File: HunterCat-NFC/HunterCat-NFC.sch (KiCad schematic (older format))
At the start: 66 parts, among them J1 Battery, J2 Breakout Conn, P1 USB_C_Plug_USB2.0, SW1 RESET, U1 ATSAMD21E18A, U2 PN7150B0HN_C11002E-PN7150B0HN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, U3 MCP73831-3-OT, U4 AP2112K-3.3, U5 GD25Q16CSIGR, Y1 27.12Mhz

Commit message: manf#
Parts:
- C1, C25: manf# (none) -> C0805C104K5RAC7800
- C10, C11: manf# (none) -> ECHU1C102GX5
- C12, C13: manf# (none) -> C1608NP0681JGT
- C14, C18: manf# (none) -> CL10C560JB8NNNC
- C15, C17: manf# (none) -> GRM1882C1H220JA01D
- C16, C23, C24: manf# (none) -> CL21A106KOQNNNG
- C19, C20: manf# (none) -> C1608C0G2E121JT000N
- C2, C5, C6, C8: manf# (none) -> 0805B105K500AT
- C21, C22: manf# (none) -> CL10C2R2BB8NNNC
- C3, C4: manf# (none) -> 0805CG100J500NT
- C7, C9: manf# (none) -> CL21B104KBCNNNC
- D1: manf# (none) -> R080508L3
- D2, D3: manf# (none) -> ORH-B35A
- D4: manf# (none) -> 2012HYK-588J
- F1: manf# (none) -> MFU0805FF00500P100
- L1, L2: manf# (none) -> MLJ1608WR16JT000
- P1: manf# (none) -> TYPE-C16PIN
- R1, R16, R2, R21: manf# (none) -> 0805W8J0103T5E
- R10, R12, R17, R18, R4: manf# (none) -> 0805W8J0102T5E
- R11, R13: manf# (none) -> RK73B1JTTD222J
- R14, R15: manf# (none) -> RC0603FR-073R4L
- R19, R20, R3, R5, R6, R7: manf# (none) -> ERJ6RBD1003V
- R8, R9: manf# (none) -> 0805W8J0512T5E
- SW1: manf# (none) -> TS-1187A-C-C-B
- U1: manf# (none) -> ATSAMD21E18A-AU
- U2: manf# (none) -> PN7150B0HN/C11002
- U3: manf# (none) -> MCP73831-3-OT
- U4: manf# (none) -> AP2112K-3.3
- U5: manf# (none) -> GD25Q16CSIGR
- Y1: manf# (none) -> X3S027120BA1H-X

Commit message: change manf#
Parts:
- C1, C25: manf# C0805C104K5RAC7800 -> 885012207072
- C10, C11: manf# ECHU1C102GX5 -> CC0201JRX7R7BB102
- C12, C13: manf# C1608NP0681JGT -> 885012206107
- C14, C18: manf# CL10C560JB8NNNC -> GRM0335C1H560FA01D
- C15, C17: manf# GRM1882C1H220JA01D -> 06035A220JAT4A
- C16, C23, C24: manf# CL21A106KOQNNNG -> C0805C106K9PACTU
- C19, C20: manf# C1608C0G2E121JT000N -> C0603C121J5GAC
- C2, C5, C6, C8: manf# 0805B105K500AT -> 885012207078
- C21, C22: manf# CL10C2R2BB8NNNC -> GCM0335C1E2R2CA16D
- C3, C4: manf# 0805CG100J500NT -> 885012007076
- C7, C9: manf# CL21B104KBCNNNC -> 885012207072
- R1, R16, R2, R21: manf# 0805W8J0103T5E -> CRCW080510K0JNEAC
- R10, R12, R17, R18, R4: manf# 0805W8J0102T5E -> CRCW08051K50FKEAC
- R11, R13: manf# RK73B1JTTD222J -> RC0603JR-072K2L
- R3, R5, R6, R7: manf# ERJ6RBD1003V -> CRCW0805100KFKEAC
- R8, R9: manf# 0805W8J0512T5E -> CR0805-FX-5101ELF

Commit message: Change sch
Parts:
- added GPIO1: RESET, Button_Switch_SMD:SW_SPST_TL3342, symbol Switch:SW_Push
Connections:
- net GND: now also GPIO1.1
- net GPIO: now reaches U1.17 (PA16/I2C/EINT0/SERCOM1+3.0)
- net GPIO: now also GPIO1.2
- no-connect marks 10 -> 9
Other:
- moved on the sheet: D1, D3, D4, R17, R18, R4, SW1
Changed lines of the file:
@@
 EESchema Schematic File Version 4
-LIBS:HunterCat-NFC-cache
 EELAYER 30 0
 EELAYER END
@@
 L Switch:SW_Push SW1
 U 1 1 5E4BA999
-P 4665 3790
-F 0 "SW1" H 4665 4075 50  0000 C CNN
-F 1 "RESET" H 4665 3984 50  0000 C CNN
-F 2 "Button_Switch_SMD:SW_SPST_TL3342" H 4665 3990 50  0001 C CNN
-F 3 "~" H 4665 3990 50  0001 C CNN
-F 4 "TS-1187A-C-C-B" H 4665 3790 50  0001 C CNN "manf#"
-	1    4665 3790
+P 4640 3765
+F 0 "SW1" H 4640 4050 50  0000 C CNN
+F 1 "RESET" H 4640 3959 50  0000 C CNN
+F 2 "Button_Switch_SMD:SW_SPST_TL3342" H 4640 3965 50  0001 C CNN
+F 3 "~" H 4640 3965 50  0001 C CNN
+F 4 "TS-1187A-C-C-B" H 4640 3765 50  0001 C CNN "manf#"
+	1    4640 3765
 	1    0    0    -1
 $EndComp
@@
 L Device:LED D1
 U 1 1 5E4BB3C2
-P 4735 4380
-F 0 "D1" H 4728 4596 50  0000 C CNN
-F 1 "LED" H 4728 4505 50  0000 C CNN
-F 2 "LED_SMD:LED_0805_2012Metric_Pad1.15x1.40mm_HandSolder" H 4735 4380 50  0001 C CNN
-F 3 "~" H 4735 4380 50  0001 C CNN
-F 4 "R080508L3" H 4735 4380 50  0001 C CNN "manf#"
-	1    4735 4380
+P 4585 4780
+F 0 "D1" H 4578 4996 50  0000 C CNN
+F 1 "LED" H 4578 4905 50  0000 C CNN
+F 2 "LED_SMD:LED_0805_2012Metric_Pad1.15x1.40mm_HandSolder" H 4585 4780 50  0001 C CNN
+F 3 "~" H 4585 4780 50  0001 C CNN
+F 4 "R080508L3" H 4585 4780 50  0001 C CNN "manf#"
+	1    4585 4780
 	1    0    0    -1
 $EndComp
@@
 L Device:R_Small R4
 U 1 1 5E4BBC69
-P 4405 4380
-F 0 "R4" V 4209 4380 50  0000 C CNN
-F 1 "1K" V 4300 4380 50  0000 C CNN
-F 2 "Resistor_SMD:R_0805_2012Metric_Pad1.15x1.40mm_HandSolder" H 4405 4380 50  0001 C CNN
-F 3 "~" H 4405 4380 50  0001 C CNN
-F 4 "CRCW08051K50FKEAC" H 4405 4380 50  0001 C CNN "manf#"
-	1    4405 4380
+P 4255 4780
+F 0 "R4" V 4059 4780 50  0000 C CNN
+F 1 "1K" V 4150 4780 50  0000 C CNN
+F 2 "Resistor_SMD:R_0805_2012Metric_Pad1.15x1.40mm_HandSolder" H 4255 4780 50  0001 C CNN
+F 3 "~" H 4255 4780 50  0001 C CNN
+F 4 "CRCW08051K50FKEAC" H 4255 4780 50  0001 C CNN "manf#"
+	1    4255 4780
 	0    1    1    0
 $EndComp
 Wire Wire Line
-	4585 4380 4505 4380
-Wire Wire Line
-	4305 4380 4210 4380
-Wire Wire Line
-	4210 4380 4210 4420
-Wire Wire Line
-	4885 4380 4965 4380
+	4435 4780 4355 4780
+Wire Wire Line
+	4155 4780 4060 4780
+Wire Wire Line
+	4060 4780 4060 4820
+Wire Wire Line
+	4735 4780 4815 4780
 $Comp
 L power:GND #PWR011
 U 1 1 5E4CF1CD
-P 4210 4420
-F 0 "#PWR011" H 4210 4170 50  0001 C CNN
-F 1 "GND" H 4215 4247 50  0000 C CNN
-F 2 "" H 4210 4420 50  0001 C CNN
-F 3 "" H 4210 4420 50  0001 C CNN
-	1    4210 4420
-	1    0    0    -1
-$EndComp
-Text Label 4965 4380 0    50   ~ 0
+P 4060 4820
+F 0 "#PWR011" H 4060 4570 50  0001 C CNN
+F 1 "GND" H 4065 4647 50  0000 C CNN
+F 2 "" H 4060 4820 50  0001 C CNN
+F 3 "" H 4060 4820 50  0001 C CNN
+	1    4060 4820
+	1    0    0    -1
+$EndComp
+Text Label 4815 4780 0    50   ~ 0
 LED1
 Wire Wire Line
@@
 LED1
 Wire Wire Line
-	4465 3790 4385 3790
-Wire Wire Line
-	4385 3790 4385 3825
-Wire Wire Line
-	4865 3790 4940 3790
-Text Label 4940 3790 0    50   ~ 0
+	4440 3765 4360 3765
+Wire Wire Line
+	4360 3765 4360 3800
+Wire Wire Line
+	4840 3765 4915 3765
+Text Label 4915 3765 0    50   ~ 0
 RESET
 $Comp
 L power:GND #PWR013
 U 1 1 5E4EA915
-P 4385 3825
-F 0 "#PWR013" H 4385 3575 50  0001 C CNN
-F 1 "GND" H 4390 3652 50  0000 C CNN
-F 2 "" H 4385 3825 50  0001 C CNN
-F 3 "" H 4385 3825 50  0001 C CNN
-	1    4385 3825
+P 4360 3800
+F 0 "#PWR013" H 4360 3550 50  0001 C CNN
+F 1 "GND" H 4365 3627 50  0000 C CNN
+F 2 "" H 4360 3800 50  0001 C CNN
+F 3 "" H 4360 3800 50  0001 C CNN
+	1    4360 3800
 	1    0    0    -1
 $EndComp
@@
 L Device:LED D3
 U 1 1 5E770C69
-P 4750 4810
-F 0 "D3" H 4743 5026 50  0000 C CNN
-F 1 "LED" H 4743 4935 50  0000 C CNN
-F 2 "LED_SMD:LED_0805_2012Metric_Pad1.15x1.40mm_HandSolder" H 4750 4810 50  0001 C CNN
-F 3 "~" H 4750 4810 50  0001 C CNN
-F 4 "ORH-B35A" H 4750 4810 50  0001 C CNN "manf#"
-	1    4750 4810
+P 4620 5135
+F 0 "D3" H 4613 5351 50  0000 C CNN
+F 1 "LED" H 4613 5260 50  0000 C CNN
+F 2 "LED_SMD:LED_0805_2012Metric_Pad1.15x1.40mm_HandSolder" H 4620 5135 50  0001 C CNN
+F 3 "~" H 4620 5135 50  0001 C CNN
+F 4 "ORH-B35A" H 4620 5135 50  0001 C CNN "manf#"
+	1    4620 5135
 	1    0    0    -1
 $EndComp
@@
 L Device:R_Small R17
 U 1 1 5E770C6F
-P 4420 4810
-F 0 "R17" V 4224 4810 50  0000 C CNN
-F 1 "1K" V 4315 4810 50  0000 C CNN
-F 2 "Resistor_SMD:R_0805_2012Metric_Pad1.15x1.40mm_HandSolder" H 4420 4810 50  0001 C CNN
-F 3 "~" H 4420 4810 50  0001 C CNN
-F 4 "CRCW08051K50FKEAC" H 4420 4810 50  0001 C CNN "manf#"
-	1    4420 4810
+P 4290 5135
+F 0 "R17" V 4094 5135 50  0000 C CNN
+F 1 "1K" V 4185 5135 50  0000 C CNN
+F 2 "Resistor_SMD:R_0805_2012Metric_Pad1.15x1.40mm_HandSolder" H 4290 5135 50  0001 C CNN
+F 3 "~" H 4290 5135 50  0001 C CNN
+F 4 "CRCW08051K50FKEAC" H 4290 5135 50  0001 C CNN "manf#"
+	1    4290 5135
 	0    1    1    0
 $EndComp
 Wire Wire Line
-	4600 4810 4520 4810
-Wire Wire Line
-	4320 4810 4225 4810
-Wire Wire Line
-	4225 4810 4225 4850
-Wire Wire Line
-	4900 4810 4980 4810
+	4470 5135 4390 5135
+Wire Wire Line
+	4190 5135 4095 5135
+Wire Wire Line
+	4095 5135 4095 5175
+Wire Wire Line
+	4770 5135 4850 5135
 $Comp
 L power:GND #PWR0103
 U 1 1 5E770C79
-P 4225 4850
-F 0 "#PWR0103" H 4225 4600 50  0001 C CNN
-F 1 "GND" H 4230 4677 50  0000 C CNN
-F 2 "" H 4225 4850 50  0001 C CNN
-F 3 "" H 4225 4850 50  0001 C CNN
-	1    4225 4850
-	1    0    0    -1
-$EndComp
-Text Label 4980 4810 0    50   ~ 0
+P 4095 5175
+F 0 "#PWR0103" H 4095 4925 50  0001 C CNN
+F 1 "GND" H 4100 5002 50  0000 C CNN
+F 2 "" H 4095 5175 50  0001 C CNN
+F 3 "" H 4095 5175 50  0001 C CNN
+	1    4095 5175
+	1    0    0    -1
+$EndComp
+Text Label 4850 5135 0    50   ~ 0
 LED2
 $Comp
 L Device:LED D4
 U 1 1 5E793493
-P 4755 5355
-F 0 "D4" H 4748 5571 50  0000 C CNN
-F 1 "LED" H 4748 5480 50  0000 C CNN
-F 2 "LED_SMD:LED_0805_2012Metric_Pad1.15x1.40mm_HandSolder" H 4755 5355 50  0001 C CNN
-F 3 "~" H 4755 5355 50  0001 C CNN
-F 4 "2012HYK-588J" H 4755 5355 50  0001 C CNN "manf#"
-	1    4755 5355
+P 4645 5540
+F 0 "D4" H 4638 5756 50  0000 C CNN
+F 1 "LED" H 4638 5665 50  0000 C CNN
+F 2 "LED_SMD:LED_0805_2012Metric_Pad1.15x1.40mm_HandSolder" H 4645 5540 50  0001 C CNN
+F 3 "~" H 4645 5540 50  0001 C CNN
+F 4 "2012HYK-588J" H 4645 5540 50  0001 C CNN "manf#"
+	1    4645 5540
 	1    0    0    -1
 $EndComp
@@
 L Device:R_Small R18
 U 1 1 5E793499
-P 4425 5355
-F 0 "R18" V 4229 5355 50  0000 C CNN
-F 1 "1K" V 4320 5355 50  0000 C CNN
-F 2 "Resistor_SMD:R_0805_2012Metric_Pad1.15x1.40mm_HandSolder" H 4425 5355 50  0001 C CNN
-F 3 "~" H 4425 5355 50  0001 C CNN
-F 4 "CRCW08051K50FKEAC" H 4425 5355 50  0001 C CNN "manf#"
-	1    4425 5355
+P 4315 5540
+F 0 "R18" V 4119 5540 50  0000 C CNN
+F 1 "1K" V 4210 5540 50  0000 C CNN
+F 2 "Resistor_SMD:R_0805_2012Metric_Pad1.15x1.40mm_HandSolder" H 4315 5540 50  0001 C CNN
+F 3 "~" H 4315 5540 50  0001 C CNN
+F 4 "CRCW08051K50FKEAC" H 4315 5540 50  0001 C CNN "manf#"
+	1    4315 5540
 	0    1    1    0
 $EndComp
 Wire Wire Line
-	4605 5355 4525 5355
-Wire Wire Line
-	4325 5355 4230 5355
-Wire Wire Line
-	4230 5355 4230 5395
-Wire Wire Line
-	4905 5355 4985 5355
+	4495 5540 4415 5540
+Wire Wire Line
+	4215 5540 4120 5540
+Wire Wire Line
+	4120 5540 4120 5580
+Wire Wire Line
+	4795 5540 4875 5540
 $Comp
 L power:GND #PWR0104
 U 1 1 5E7934A3
-P 4230 5395
-F 0 "#PWR0104" H 4230 5145 50  0001 C CNN
-F 1 "GND" H 4235 5222 50  0000 C CNN
-F 2 "" H 4230 5395 50  0001 C CNN
-F 3 "" H 4230 5395 50  0001 C CNN
-	1    4230 5395
-	1    0    0    -1
-$EndComp
-Text Label 4985 5355 0    50   ~ 0
+P 4120 5580
+F 0 "#PWR0104" H 4120 5330 50  0001 C CNN
+F 1 "GND" H 4125 5407 50  0000 C CNN
+F 2 "" H 4120 5580 50  0001 C CNN
+F 3 "" H 4120 5580 50  0001 C CNN
+	1    4120 5580
+	1    0    0    -1
+$EndComp
+Text Label 4875 5540 0    50   ~ 0
 LED3
 NoConn ~ 3150 4810
@@
 Text Label 3201 6810 0    50   ~ 0
 MISO
-NoConn ~ 3150 6110
 $Comp
 L hunter-cat-nfc:PN7150B0HN_C11002E-PN7150B0HN_C11002E U2
@@
 Wire Wire Line
 	8505 5870 8505 5955
+$Comp
+L Switch:SW_Push GPIO1
+U 1 1 5F214F20
+P 4570 4290
+F 0 "GPIO1" H 4570 4575 50  0000 C CNN
+F 1 "RESET" H 4570 4484 50  0000 C CNN
+F 2 "Button_Switch_SMD:SW_SPST_TL3342" H 4570 4490 50  0001 C CNN
+F 3 "~" H 4570 4490 50  0001 C CNN
+F 4 "TS-1187A-C-C-B" H 4570 4290 50  0001 C CNN "manf#"
+	1    4570 4290
+	1    0    0    -1
+$EndComp
+$Comp
+L power:GND #PWR038
+U 1 1 5F2292A9
+P 4115 4375
+F 0 "#PWR038" H 4115 4125 50  0001 C CNN
+F 1 "GND" H 4120 4202 50  0000 C CNN
+F 2 "" H 4115 4375 50  0001 C CNN
+F 3 "" H 4115 4375 50  0001 C CNN
+	1    4115 4375
+	1    0    0    -1
+$EndComp
+Text Label 4930 4290 0    50   ~ 0
+GPIO
+Wire Wire Line
+	4770 4290 4930 4290
+Wire Wire Line
+	4370 4290 4115 4290
+Wire Wire Line
+	4115 4290 4115 4375
+Text Label 3150 6110 0    50   ~ 0
+GPIO
 $EndSCHEMATC

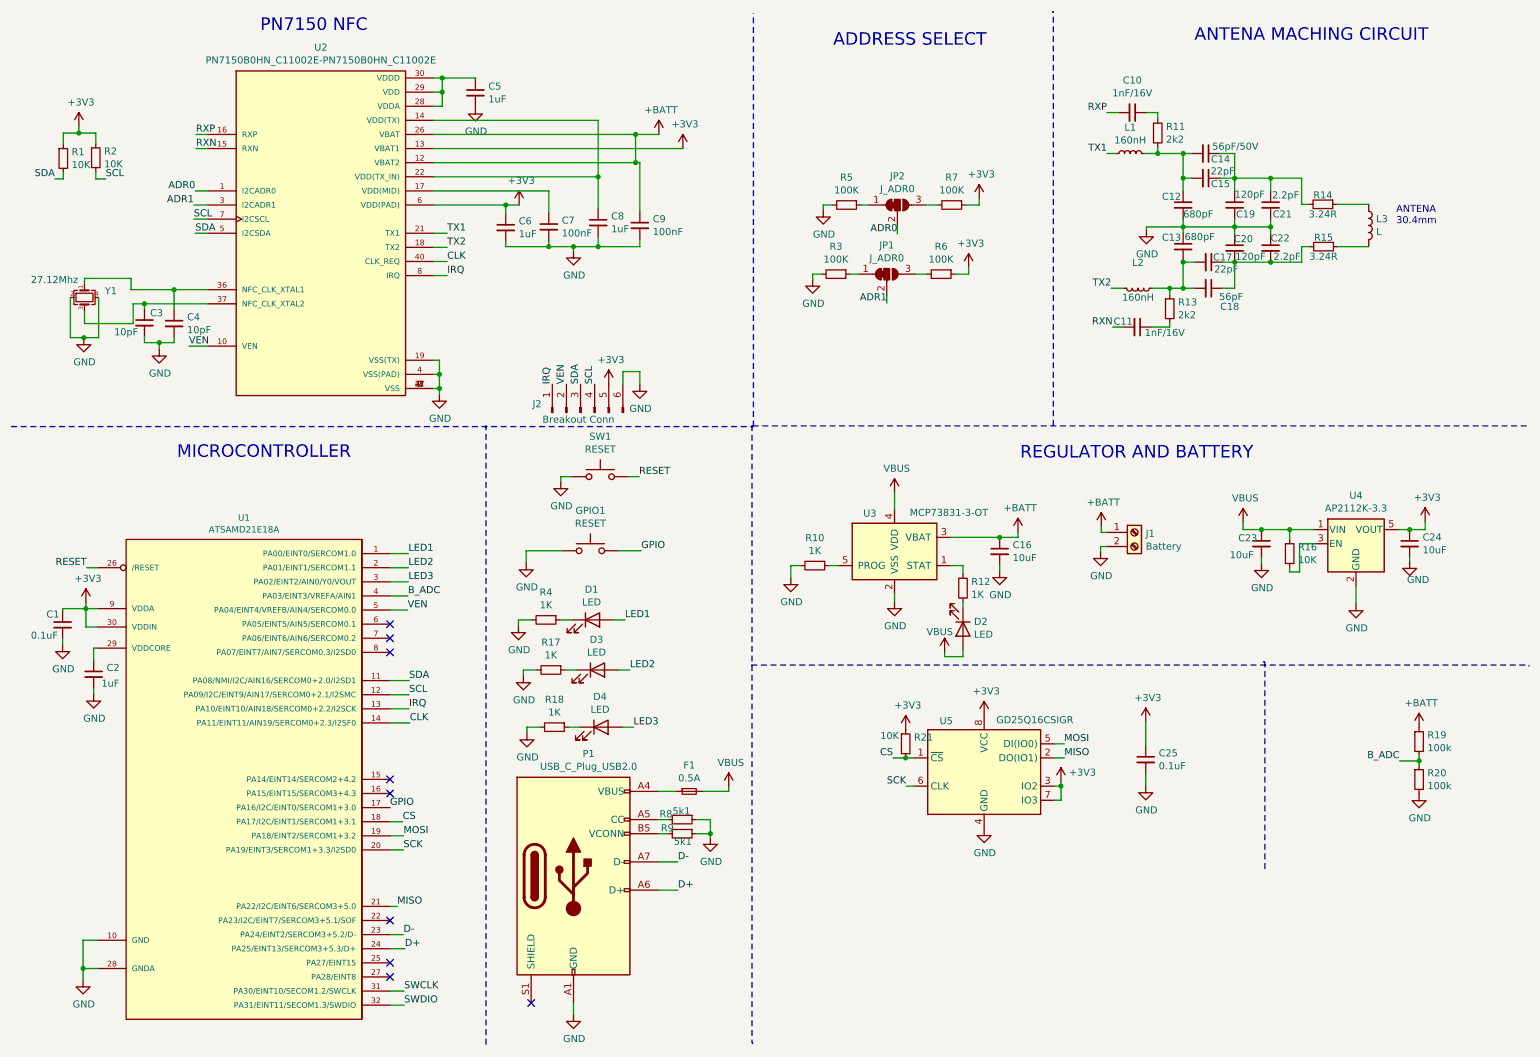
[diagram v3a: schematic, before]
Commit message: Fix Batt source
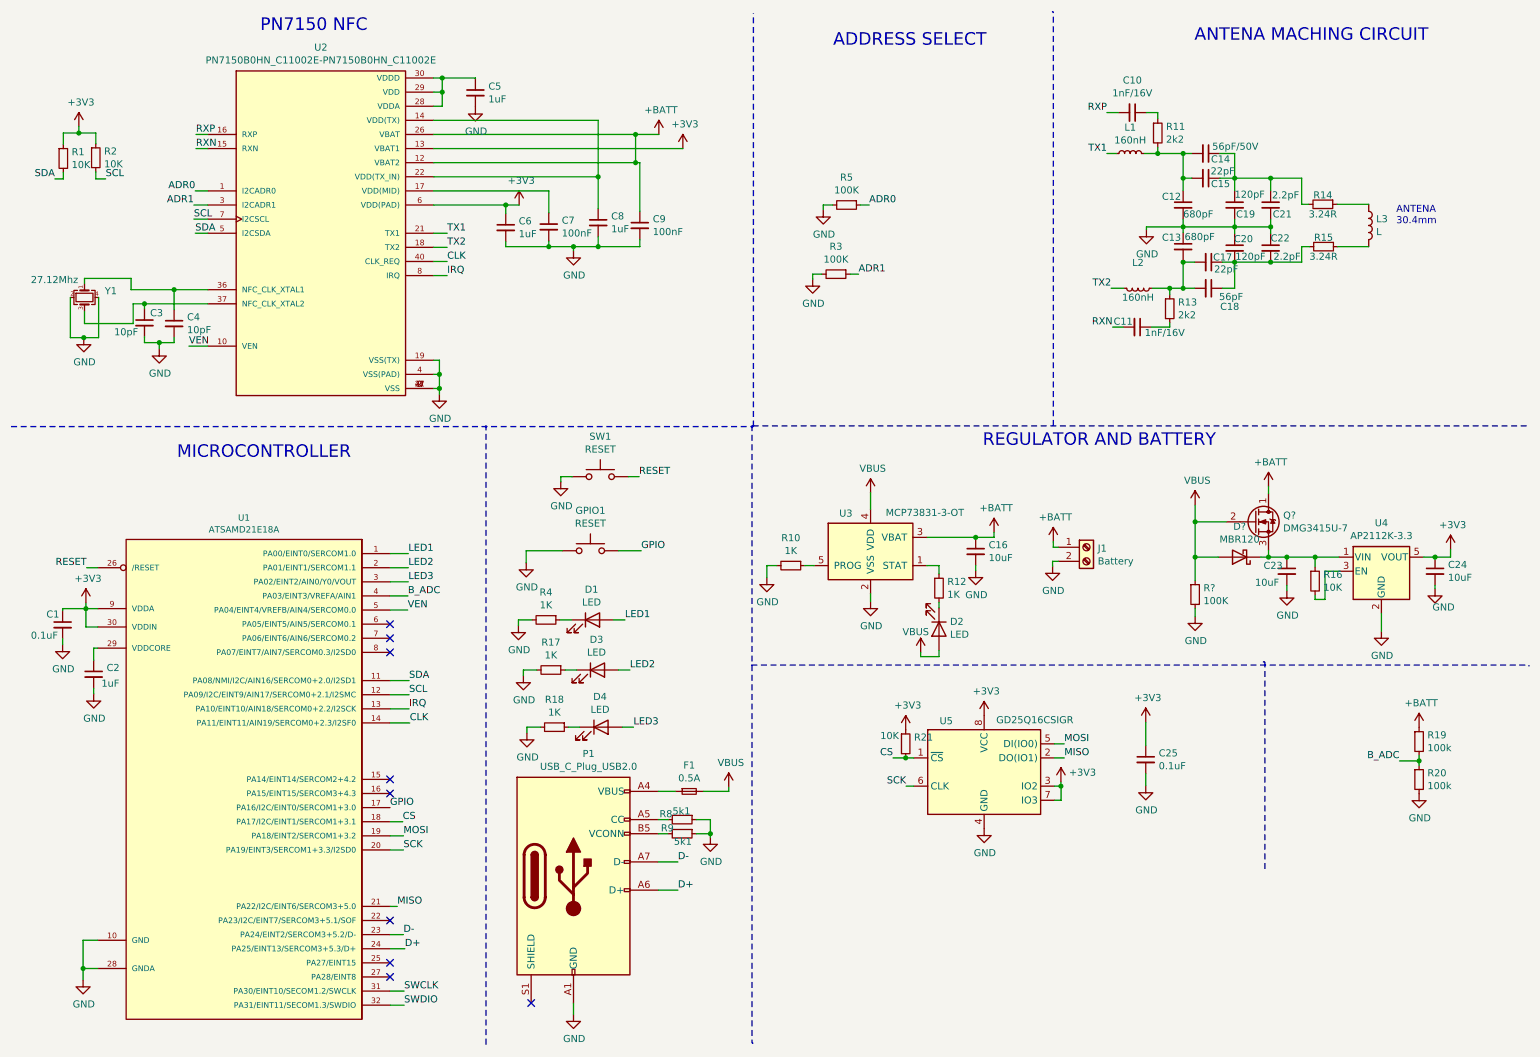
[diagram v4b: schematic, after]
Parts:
- removed J2: Breakout Conn, Connector_PinSocket_2.54mm:PinSocket_1x06_P2.54mm_Vertical, symbol Connector:Conn_01x06_Male
- removed JP1, JP2: J_ADR0, Jumper:SolderJumper-3_P1.3mm_Bridged12_RoundedPad1.0x1.5mm, symbol Jumper:SolderJumper_3_Bridged12
- removed R6, R7: 100K, Resistor_SMD:R_0805_2012Metric_Pad1.15x1.40mm_HandSolder, symbol Device:R_Small
- added D?: MBR120, Diode_THT:D_DO-201AD_P15.24mm_Horizontal, symbol Diode:MBR340
- added Q?: DMG3415U-7, Package_TO_SOT_THT:TO-92_Inline, symbol Transistor_FET:BS107
- added R?: 100K, symbol Device:R_Small
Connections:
- net +BATT: now also Q?.1 (D)
- net ADR0: now also R5.1
- net ADR1: now also R3.1
- net GND: now also R?.2
- net VBUS: now also D?.2 (A), Q?.2 (G), R?.1; no longer C23.1, R16.1, U4.1 (VIN)
- new net: C23.1, D?.1 (K), Q?.3 (S), R16.1, U4.1 (VIN)
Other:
- moved on the sheet: C16, C23, C24, D2, J1, R10, R12, R16, U3, U4

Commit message: Last change
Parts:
- added J2: Conn_01x06_Female, Connector:Tag-Connect_TC2030-IDC-NL_2x03_P1.27mm_Vertical, symbol Connector:Conn_01x06_Female
- C1, C16, C2, C23, C24, C25, C3, C4, C5, C6, C7, C8, C9: footprint Capacitor_SMD:C_0805_2012Metric_Pad1.15x1.40mm_HandSolder -> Capacitor_SMD:C_0603_1608Metric_Pad1.05x0.95mm_HandSolder
- D5: renamed from D?; footprint Diode_THT:D_DO-201AD_P15.24mm_Horizontal -> Diode_SMD:D_SOD-123F
- F1: footprint Fuse:Fuse_0805_2012Metric_Pad1.15x1.40mm_HandSolder -> Fuse:Fuse_0603_1608Metric_Pad1.05x0.95mm_HandSolder
- Q1: renamed from Q?; footprint Package_TO_SOT_THT:TO-92_Inline -> Package_TO_SOT_SMD:TSOT-23
- R1, R10, R12, R16, R17, R18, R19, R2, R20, R21, R3, R4, R5, R8, R9: footprint Resistor_SMD:R_0805_2012Metric_Pad1.15x1.40mm_HandSolder -> Resistor_SMD:R_0603_1608Metric_Pad1.05x0.95mm_HandSolder
- R6: renamed from R?; footprint (none) -> Resistor_SMD:R_0603_1608Metric_Pad1.05x0.95mm_HandSolder
- U1: footprint Package_QFP:TQFP-32_7x7mm_P0.8mm -> Package_DFN_QFN:QFN-32-1EP_5x5mm_P0.5mm_EP3.6x3.6mm; manf# ATSAMD21E18A-AU -> ATSAMD21E18A-MUT
- U5: value GD25Q16CSIGR -> GD25Q16CEIGR; footprint Package_SO:SOIC-8_5.23x5.23mm_P1.27mm -> USON:USON-8; manf# GD25Q16CSIGR -> GD25Q16CEIGR
- Y1: footprint Crystal:Crystal_SMD_3225-4Pin_3.2x2.5mm_HandSoldering -> Crystal:Crystal_SMD_2520-4Pin_2.5x2.0mm; manf# X3S027120BA1H-X -> Q24FA20H00431
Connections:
- net +3V3: now also J2.1 (Pin_1)
- net GND: now also J2.5 (Pin_5)
- net SWCLK: now also J2.4 (Pin_4)
- net SWDIO: now also J2.2 (Pin_2)
- net RESET renamed RST
- net RST: now also J2.3 (Pin_3)
- no-connect marks 9 -> 10
